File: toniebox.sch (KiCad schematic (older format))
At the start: 130 parts, among them K2 Micro_SD_Card_Det_Hirose_DM3CS, K4 B3B-ZR-SM4-TF, K8 B3B-PH-SM4-TB, K9 B3B-PH-SM4-TB, T11 FDV301N, T360 FDV301N, T4 FDV301N, T5 FDV301N, T6 FDV301N, T7 FDV301N, U1 TLV320DAC3100, U2 CC3200R1M2RGCR, U3 IS25LQ032B-JNLE, U4 MMA8451QT, U8 AP2112K-3.3, U9 AP2120N-1.8

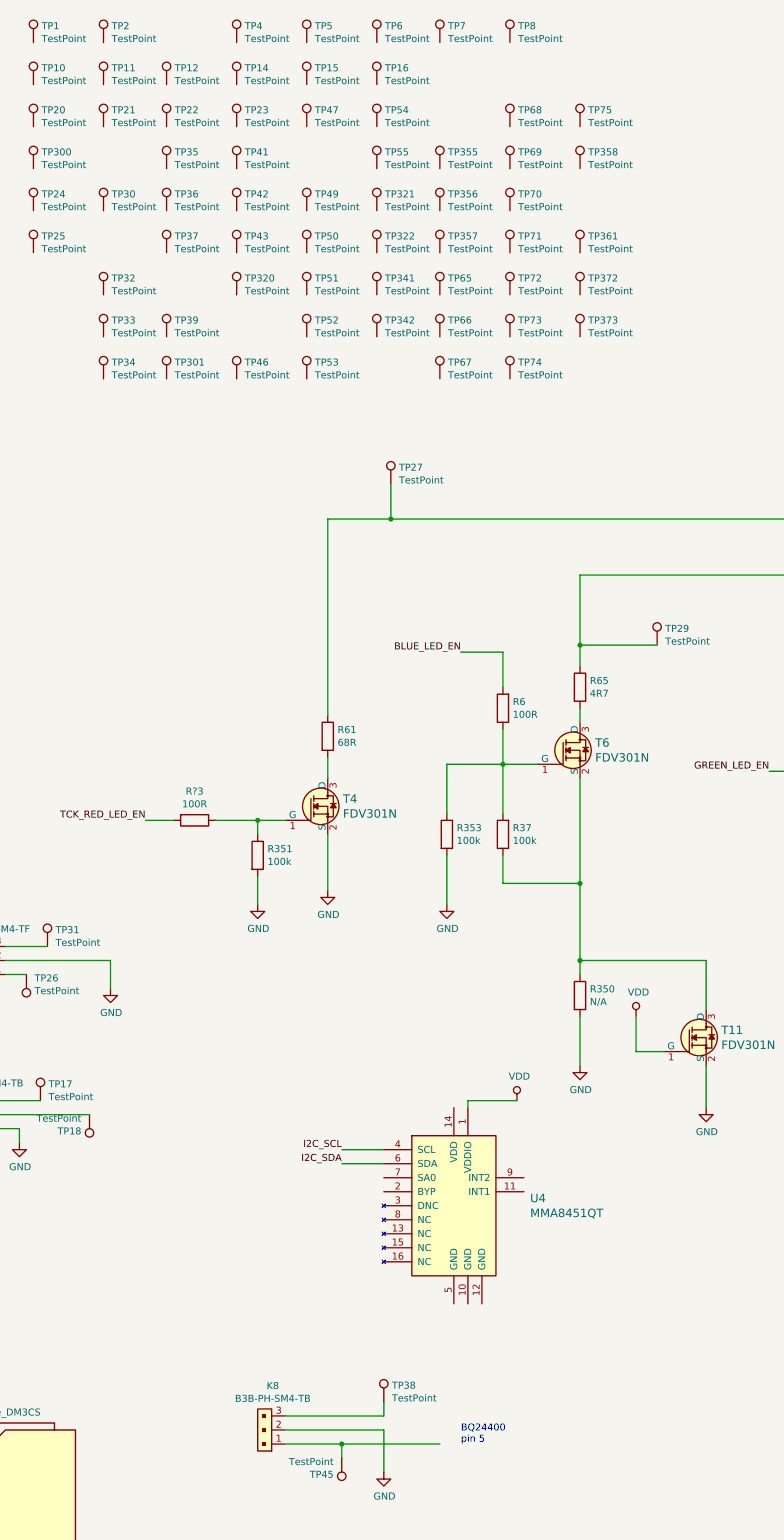
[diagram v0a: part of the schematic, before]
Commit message: battery, ear connectors;datasheets
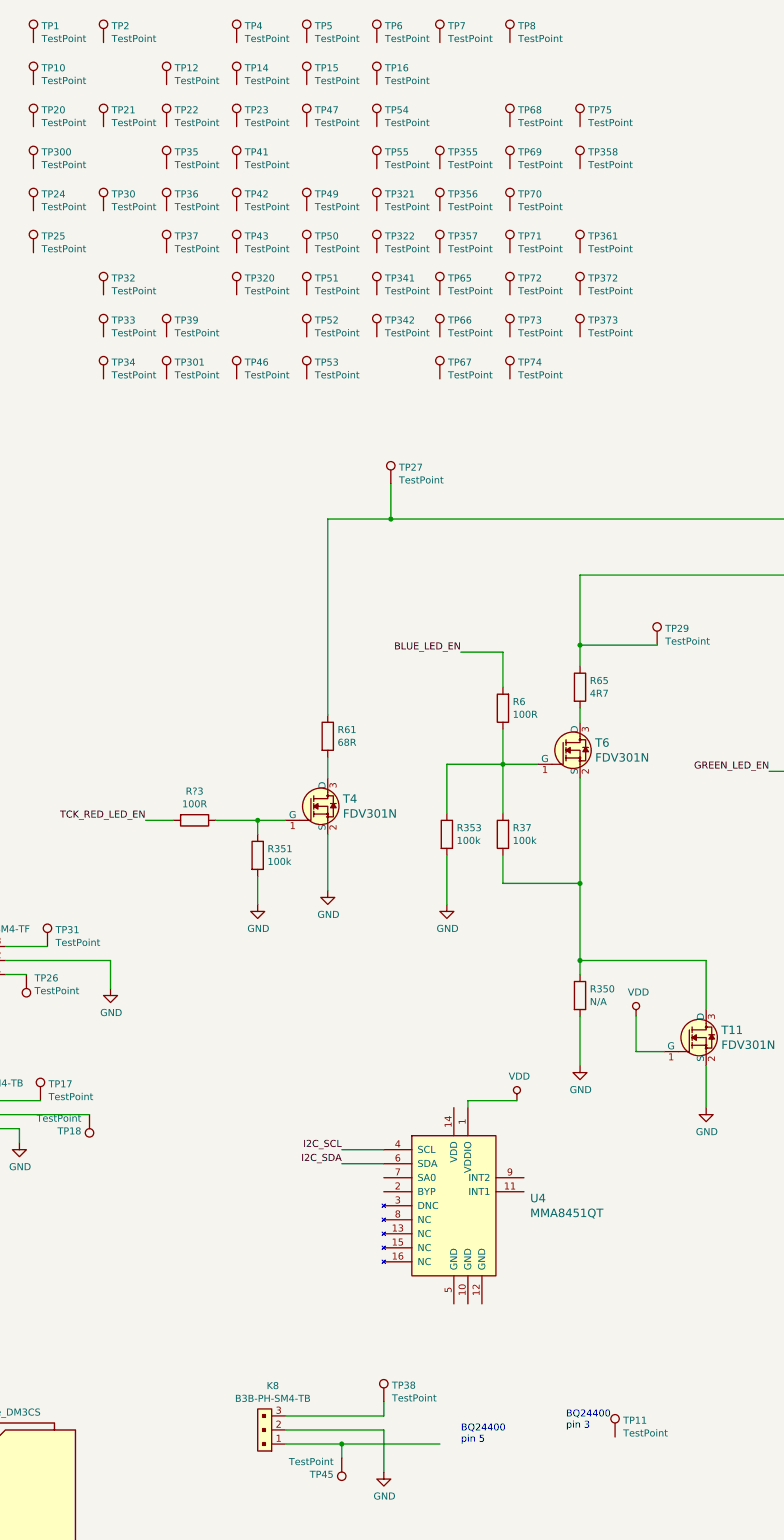
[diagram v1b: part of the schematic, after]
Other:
- note added: "BQ24400\npin 3\n"
- moved on the sheet: TP11
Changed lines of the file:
@@
 L Connector:TestPoint TP11
 U 1 1 5E30EB8B
-P 7000 1300
-F 0 "TP11" H 7058 1418 50  0000 L CNN
-F 1 "TestPoint" H 7058 1327 50  0000 L CNN
-F 2 "" H 7200 1300 50  0001 C CNN
-F 3 "~" H 7200 1300 50  0001 C CNN
-	1    7000 1300
+P 10650 10950
+F 0 "TP11" H 10708 11068 50  0000 L CNN
+F 1 "TestPoint" H 10708 10977 50  0000 L CNN
+F 2 "" H 10850 10950 50  0001 C CNN
+F 3 "~" H 10850 10950 50  0001 C CNN
+	1    10650 10950
 	1    0    0    -1
 $EndComp
@@
 	0    1    -1   0
 $EndComp
+Text Notes 10300 10900 0    50   ~ 0
+BQ24400\npin 3\n
 $EndSCHEMATC
